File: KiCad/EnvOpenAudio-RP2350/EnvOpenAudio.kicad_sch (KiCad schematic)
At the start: 72 parts, among them J1 USB_C_Receptacle_USB2.0, J2 SM03B-SRSS-TB, J3 Conn_01x10, SW1 B3U-1000, SW2 B3U-1000, U1 W25Q16JVUXIQ, U2 TPS63001DRCR, U3 TLV75518PDBV, U4 RP2350_60QFN, U5 TLV320AIC3100, U6 LM3880, Y1 ABM8-272-T3

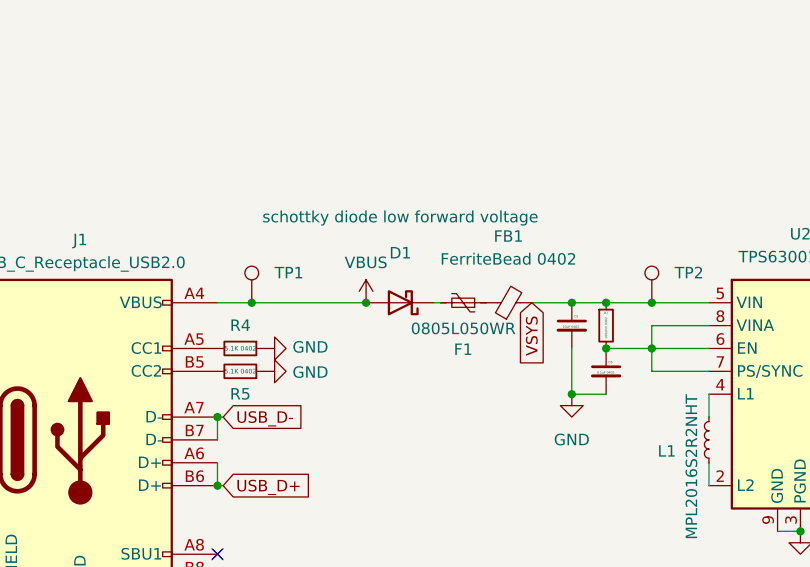
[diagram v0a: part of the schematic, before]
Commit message: Seperated into RP2040 and RP2350 variants
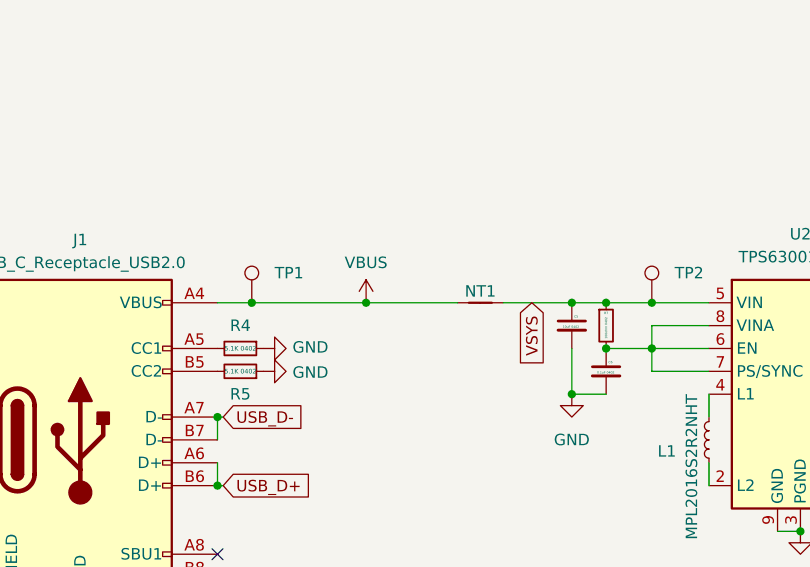
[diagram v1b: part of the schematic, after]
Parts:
- removed D1: schottky diode low forward voltage, Diode_SMD:D_SOD-123, symbol Device:D_Schottky
- removed F1: 0805L050WR, Fuse:Fuse_0805_2012Metric, symbol Device:Polyfuse_Small
- removed FB1: FerriteBead 0402, Resistor_SMD:R_0402_1005Metric, symbol Device:FerriteBead_Small
- added NT1: NetTie_2, NetTie:NetTie-2_SMD_Pad2.0mm, symbol Device:NetTie_2
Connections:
- net VBUS: now also NT1.1
- net VSYS: now also NT1.2
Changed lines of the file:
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@@
 	)
 	(junction
-		(at 57.15 22.86)
-		(diameter 0)
-		(color 0 0 0 0)
-	)
-	(junction
 		(at 187.325 132.715)
 		(diameter 0)
@@
 	)
 	(junction
+		(at 57.15 22.86)
+		(diameter 0)
+		(color 0 0 0 0)
+	)
+	(junction
 		(at 107.315 154.305)
 		(diameter 0)
@@
 	(wire
 		(pts
+			(xy 72.39 22.86) (xy 80.01 22.86)
+		)
+		(stroke
+			(width 0)
+			(type default)
+		)
+	)
+	(wire
+		(pts
 			(xy 144.78 22.86) (xy 151.13 22.86)
 		)
@@
 	(wire
 		(pts
+			(xy 57.15 22.86) (xy 67.31 22.86)
+		)
+		(stroke
+			(width 0)
+			(type default)
+		)
+	)
+	(wire
+		(pts
 			(xy 165.735 132.715) (xy 168.275 132.715)
 		)
@@
 	(wire
 		(pts
-			(xy 75.565 22.86) (xy 80.01 22.86)
-		)
-		(stroke
-			(width 0)
-			(type default)
-		)
-	)
-	(wire
-		(pts
 			(xy 217.805 208.915) (xy 233.045 208.915)
 		)
@@
 	(wire
 		(pts
-			(xy 64.77 22.86) (xy 65.405 22.86)
-		)
-		(stroke
-			(width 0)
-			(type default)
-		)
-	)
-	(wire
-		(pts
 			(xy 257.175 123.825) (xy 245.745 123.825)
 		)
@@
 	)
 	(symbol
-		(lib_id "Device:D_Schottky")
-		(at 60.96 22.86 180)
-		(unit 1)
-		(exclude_from_sim no)
-		(in_bom yes)
-		(on_board yes)
-		(dnp no)
-		(property "Reference" "D1"
-			(at 60.96 17.3482 0)
-			(effects
-				(font
-					(size 1.27 1.27)
-				)
-			)
-		)
-		(property "Value" "schottky diode low forward voltage"
-			(at 60.96 13.335 0)
-			(effects
-				(font
-					(size 1.27 1.27)
-				)
-			)
-		)
-		(property "Footprint" "Diode_SMD:D_SOD-123"
-			(at 60.96 22.86 0)
-			(effects
-				(font
-					(size 1.27 1.27)
-				)
-				(hide yes)
-			)
-		)
-		(property "Datasheet" ""
-			(at 60.96 22.86 0)
-			(effects
-				(font
-					(size 1.27 1.27)
-				)
-				(hide yes)
-			)
-		)
-		(property "Description" ""
-			(at 60.96 22.86 0)
-			(effects
-				(font
-					(size 1.27 1.27)
-				)
-				(hide yes)
-			)
-		)
-		(property "LCSC" " "
-			(at 60.96 22.86 0)
-			(effects
-				(font
-					(size 1.27 1.27)
-				)
-				(hide yes)
-			)
-		)
-		(pin "1"
-		)
-		(pin "2"
-		)
-		(instances
-			(project "EnvOpenAudio"
-				(path "/7b892ee5-f34f-4bca-8f87-a56522432f7c"
-					(reference "D1")
-					(unit 1)
-				)
-			)
-		)
-	)
-	(symbol
-		(lib_id "Device:Polyfuse_Small")
-		(at 67.945 22.86 270)
-		(mirror x)
-		(unit 1)
-		(exclude_from_sim no)
-		(in_bom yes)
-		(on_board yes)
-		(dnp no)
-		(property "Reference" "F1"
-			(at 67.945 28.067 90)
-			(effects
-				(font
-					(size 1.27 1.27)
-				)
-			)
-		)
-		(property "Value" "0805L050WR"
-			(at 67.945 25.7556 90)
-			(effects
-				(font
-					(size 1.27 1.27)
-				)
-			)
-		)
-		(property "Footprint" "Fuse:Fuse_0805_2012Metric"
-			(at 62.865 21.59 0)
-			(effects
-				(font
-					(size 1.27 1.27)
-				)
-				(justify left)
-				(hide yes)
-			)
-		)
-		(property "Datasheet" "~"
-			(at 67.945 22.86 0)
-			(effects
-				(font
-					(size 1.27 1.27)
-				)
-				(hide yes)
-			)
-		)
-		(property "Description" ""
-			(at 67.945 22.86 0)
-			(effects
-				(font
-					(size 1.27 1.27)
-				)
-				(hide yes)
-			)
-		)
-		(pin "1"
-		)
-		(pin "2"
-		)
-		(instances
-			(project "EnvOpenAudio"
-				(path "/7b892ee5-f34f-4bca-8f87-a56522432f7c"
-					(reference "F1")
-					(unit 1)
-				)
-			)
-		)
-	)
-	(symbol
 		(lib_id "Device:C_Small")
 		(at 365.76 60.96 0)
@@
 	)
 	(symbol
+		(lib_id "Device:NetTie_2")
+		(at 69.85 22.86 0)
+		(unit 1)
+		(exclude_from_sim no)
+		(in_bom no)
+		(on_board yes)
+		(dnp no)
+		(property "Reference" "NT1"
+			(at 69.85 21.59 0)
+			(effects
+				(font
+					(size 1.27 1.27)
+				)
+			)
+		)
+		(property "Value" "NetTie_2"
+			(at 69.85 20.32 0)
+			(effects
+				(font
+					(size 1.27 1.27)
+				)
+				(hide yes)
+			)
+		)
+		(property "Footprint" "NetTie:NetTie-2_SMD_Pad2.0mm"
+			(at 69.85 22.86 0)
+			(effects
+				(font
+					(size 1.27 1.27)
+				)
+				(hide yes)
+			)
+		)
+		(property "Datasheet" "~"
+			(at 69.85 22.86 0)
+			(effects
+				(font
+					(size 1.27 1.27)
+				)
+				(hide yes)
+			)
+		)
+		(property "Description" "Net tie, 2 pins"
+			(at 69.85 22.86 0)
+			(effects
+				(font
+					(size 1.27 1.27)
+				)
+				(hide yes)
+			)
+		)
+		(pin "1"
+		)
+		(pin "2"
+		)
+		(instances
+			(project ""
+				(path "/7b892ee5-f34f-4bca-8f87-a56522432f7c"
+					(reference "NT1")
+					(unit 1)
+				)
+			)
+		)
+	)
+	(symbol
 		(lib_id "power:GND")
 		(at 72.39 185.42 0)
@@
 					(unit 1)
 				)
-			)
-		)
-	)
-	(symbol
-		(lib_id "Device:FerriteBead_Small")
-		(at 73.025 22.86 90)
-		(unit 1)
-		(exclude_from_sim no)
-		(in_bom yes)
-		(on_board yes)
-		(dnp no)
-		(fields_autoplaced yes)
-		(property "Reference" "FB1"
-			(at 72.9742 15.494 90)
-			(effects
-				(font
-					(size 1.27 1.27)
-				)
-			)
-		)
-		(property "Value" "FerriteBead 0402"
-			(at 72.9742 18.034 90)
-			(effects
-				(font
-					(size 1.27 1.27)
-				)
-			)
-		)
-		(property "Footprint" "Resistor_SMD:R_0402_1005Metric"
-			(at 73.025 24.638 90)
-			(effects
-				(font
-					(size 1.27 1.27)
-				)
-				(hide yes)
-			)
-		)
-		(property "Datasheet" "~"
-			(at 73.025 22.86 0)
-			(effects
-				(font
-					(size 1.27 1.27)
-				)
-				(hide yes)
-			)
-		)
-		(property "Description" ""
-			(at 73.025 22.86 0)
-			(effects
-				(font
-					(size 1.27 1.27)
-				)
-				(hide yes)
-			)
-		)
-		(pin "1"
-		)
-		(pin "2"
-		)
-		(instances
-			(project "EnvOpenAudio"
-				(path "/7b892ee5-f34f-4bca-8f87-a56522432f7c"
-					(reference "FB1")
-					(unit 1)
-				)
